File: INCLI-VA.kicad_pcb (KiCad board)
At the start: 2 copper layers, 100 x 70 mm, 155 parts, among them J1 MSTB 2,5/5-GF-5,08, J2 MSTB 2,5/2-GF-5,08, J401 USB4105-GF-A, J402 UART0, Q101 STD18NF25, Q102 IPD30N10S3L-34, Q701 FDD7N25LZ, Q702 BC817-40, Q703 BC807-40, Q751 FDD7N25LZ, Q752 BC817-40, Q753 BC807-40, SW401 RESET, SW402 BOOT, U1 ADM3055E, U101 LM74930QRGERQ1, U201 TPS7A1650QDGNRQ1, U202 ISO7763FQDWRQ1, U301 TPS62A02QDRLRQ1, U302 LP5907QMFX-3.3Q1, U401 ESP32-S3-WROOM-1-N8R2, U402 USBLC6-2SC6, U501 SCL3300-D01, U502 ASM330LHHTR, U503 AS5147U-HTSM

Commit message: [Claude Code] DRU para JLCPCB, red U101_RTN y limpieza de librerías
- INCLI-VA.kicad_dru: capacidades de JLCPCB (2 capas, 1 oz, 1.6 mm) con
  margen; separación HV en la entrada (1.25 mm, IPC-2221B B2), DO y
  +VPROT (0.6 mm); barrera del ADM3055E (2.5 mm + sin relleno bajo U601);
  anchos IPC-2152 (entrada 1.0 mm, DO y 5 V 0.5 mm); reglas para el pad 25
  de U101 (aislado y nunca GND, probado en una copia).
- U101 pin 25 (EP): no_connect -> passive en la librería y la caché;
  etiqueta U101_RTN en 10_power_input. En el PCB, las 7 redes
  unconnected-(U101-EP-Pad25)_N quedan como /10_power_input/U101_RTN
  (sin Update PCB from Schematic).
- Se borran las huellas y modelos 3D de URB2405 y HVSSOP-8, fp-lib-table.bak
  y lib/Connector_Phoenix_MSTB.pretty.bak/.
- PENDIENTES: reglas y fuentes, estado del DRC, propuesta de la hoja 80.

Co-Authored-By: Claude Opus 5.5 <noreply@anthropic.com>
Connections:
- U101 pad 25: unconnected-(U101-EP-Pad25) -> /10_power_input/U101_RTN
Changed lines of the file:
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@@
 			(layers "*.Cu")
 			(remove_unused_layers no)
-			(net "unconnected-(U101-EP-Pad25)_2")
+			(net "/10_power_input/U101_RTN")
 			(pinfunction "EP_25")
-			(pintype "no_connect")
+			(pintype "passive")
 		)
 		(pad "25" thru_hole circle
@@
 			(layers "*.Cu")
 			(remove_unused_layers no)
-			(net "unconnected-(U101-EP-Pad25)_1")
+			(net "/10_power_input/U101_RTN")
 			(pinfunction "EP_25")
-			(pintype "no_connect")
+			(pintype "passive")
 		)
 		(pad "25" thru_hole circle
@@
 			(layers "*.Cu")
 			(remove_unused_layers no)
-			(net "unconnected-(U101-EP-Pad25)_5")
+			(net "/10_power_input/U101_RTN")
 			(pinfunction "EP_25")
-			(pintype "no_connect")
+			(pintype "passive")
 		)
 		(pad "25" smd rect
@@
 			(size 2.1 2.1)
 			(layers "F.Cu" "F.Mask")
-			(net "unconnected-(U101-EP-Pad25)_4")
+			(net "/10_power_input/U101_RTN")
 			(pinfunction "EP_25")
-			(pintype "no_connect")
+			(pintype "passive")
 			(zone_connect 2)
 		)
@@
 			(size 2.4 2.4)
 			(layers "B.Cu" "B.Mask")
-			(net "unconnected-(U101-EP-Pad25)_6")
+			(net "/10_power_input/U101_RTN")
 			(pinfunction "EP_25")
-			(pintype "no_connect")
+			(pintype "passive")
 		)
 		(pad "25" thru_hole circle
@@
 			(layers "*.Cu")
 			(remove_unused_layers no)
-			(net "unconnected-(U101-EP-Pad25)_3")
+			(net "/10_power_input/U101_RTN")
 			(pinfunction "EP_25")
-			(pintype "no_connect")
+			(pintype "passive")
 		)
 		(pad "25" thru_hole circle
@@
 			(layers "*.Cu")
 			(remove_unused_layers no)
-			(net "unconnected-(U101-EP-Pad25)")
+			(net "/10_power_input/U101_RTN")
 			(pinfunction "EP_25")
-			(pintype "no_connect")
+			(pintype "passive")
 		)
 		(embedded_fonts no)

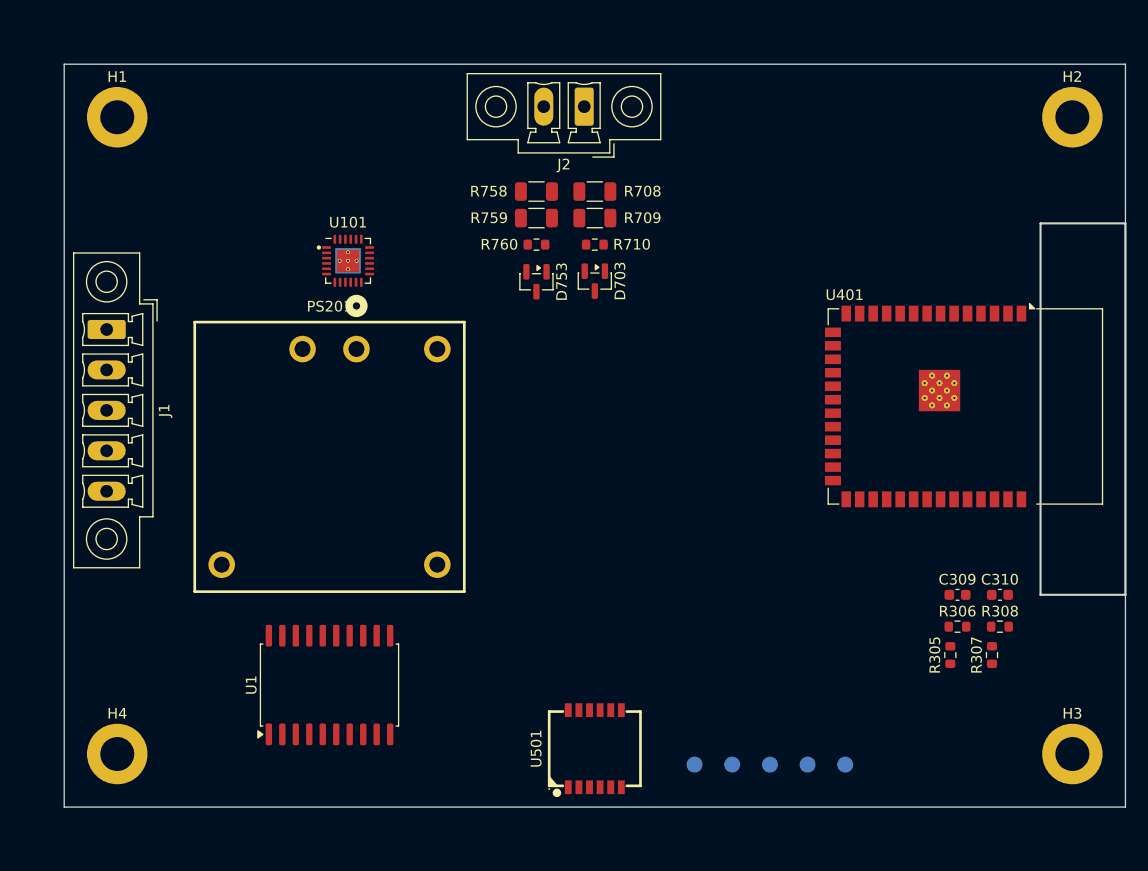
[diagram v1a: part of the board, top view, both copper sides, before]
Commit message: [Claude Code] 80_supervision: TPS3828-33-Q1, LED y VAR_ID; J1/J2 verticales; contorno con muesca
- 80_supervision: U801 TPS3828-33QDBVRQ1 (supervisor de +3V3_D + watchdog,
  WDI <- IO17), R802 0 ohm, R801 DNP; LED verde/rojo DNP en PROD (caja
  opaca); VAR_ID0/1 (CAN/OUT) y VAR_ID2 (IO8, CABIN, DNP).
- WD_EN eliminado (IO18 libre); VAR_ID2 ocupa su pin en las hojas 40/80 y la raíz.
- 10_power_input: J1/J2 MSTBV 2,5 GF 5.08 verticales (1777109 / 1777073).
- lib: se borran los símbolos URB2405 y TPS7A1650; U101: vías del EP a Ø 0.45 mm.
- PCB: contorno único con muesca de 8 x 35 mm para la antena (antes, dos
  rectángulos superpuestos); serigrafía de U401 recortada en la muesca.
- ERC: 0 errores, 1 aviso intencional (U101_RTN).

Co-Authored-By: Claude Opus 5.5 <noreply@anthropic.com>
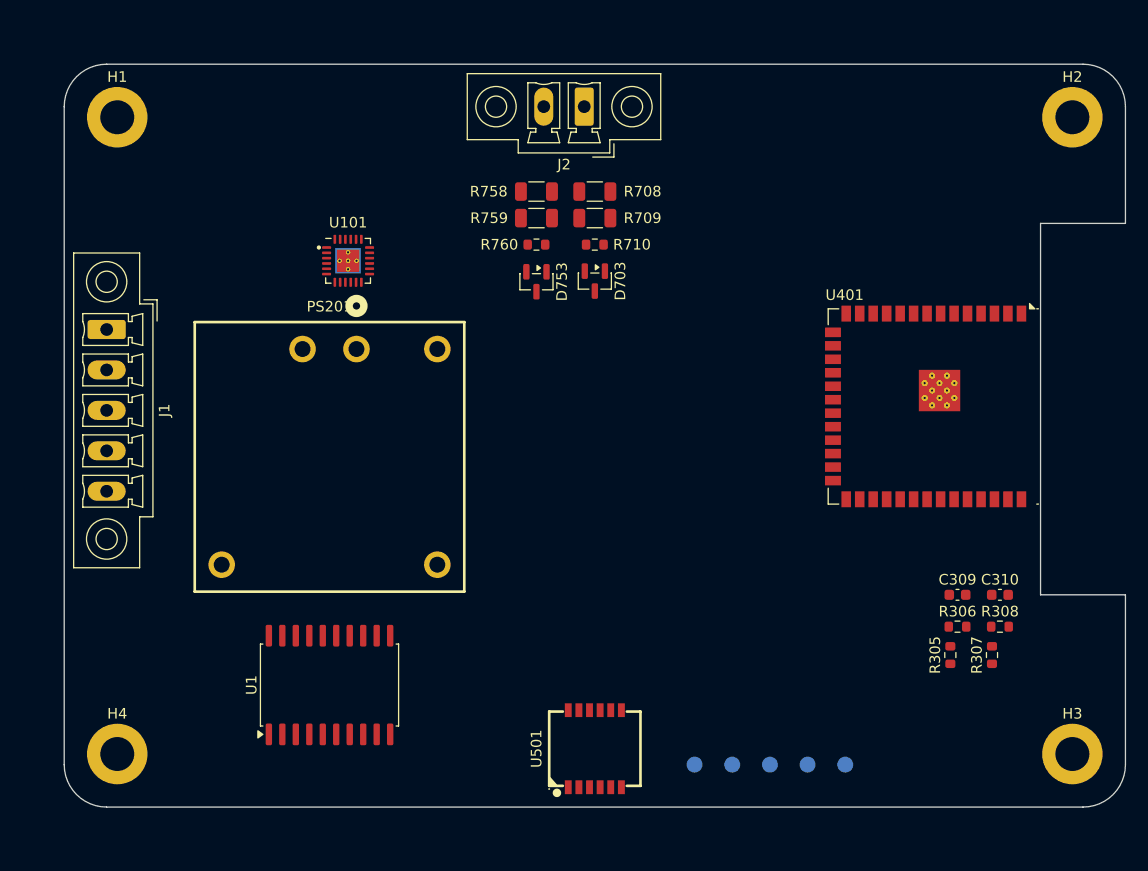
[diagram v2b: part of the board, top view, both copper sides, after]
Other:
- outline, holes or cut-outs redrawn
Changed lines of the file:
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@@
 		(layer "F.Cu")
 		(at 126.75 68.525)
-		(descr "TI LM74930-Q1 RGE0024T VQFN-24 4x4 mm, P0.5 mm, EP 2.1 mm. Fuente: datasheet TI SNOSDF6 (Oct 2023), Example Board Layout / Stencil 4228214/A. Pads alargados a 0.85 mm (TI 0.6) con el mismo borde interior para soldar a mano. Pasta del EP en 4x 0.94 mm (77 %%). 5 vias dia 0.2 mm en el EP hacia una isla aislada en B.Cu: el EP es RTN y TI pide dejarlo flotante, NO conectar a GND.")
+		(descr "TI LM74930-Q1 RGE0024T VQFN-24 4x4 mm, P0.5 mm, EP 2.1 mm. Fuente: datasheet TI SNOSDF6 (Oct 2023), Example Board Layout / Stencil 4228214/A. Pads alargados a 0.85 mm (TI 0.6) con el mismo borde interior para soldar a mano. Pasta del EP en 4x 0.94 mm (77 %%). 5 vias en el EP (hueco 0.2 mm, Ø 0.45 mm: sin recargo en JLCPCB) hacia una isla aislada en B.Cu: el EP es RTN y TI pide dejarlo flotante, NO conectar a GND.")
 		(tags "VQFN-24 RGE0024T LM74930 thermal vias hand solder")
 		(property "Reference" "U101"
@@
 		(pad "25" thru_hole circle
 			(at -0.8 0)
-			(size 0.4 0.4)
+			(size 0.45 0.45)
 			(drill 0.2)
 			(layers "*.Cu")
@@
 		(pad "25" thru_hole circle
 			(at 0 -0.8)
-			(size 0.4 0.4)
+			(size 0.45 0.45)
 			(drill 0.2)
 			(layers "*.Cu")
@@
 		(pad "25" thru_hole circle
 			(at 0 0)
-			(size 0.4 0.4)
+			(size 0.45 0.45)
 			(drill 0.2)
 			(layers "*.Cu")
@@
 		(pad "25" thru_hole circle
 			(at 0 0.8)
-			(size 0.4 0.4)
+			(size 0.45 0.45)
 			(drill 0.2)
 			(layers "*.Cu")
@@
 		(pad "25" thru_hole circle
 			(at 0.8 0)
-			(size 0.4 0.4)
+			(size 0.45 0.45)
 			(drill 0.2)
 			(layers "*.Cu")
@@
 		)
 		(fp_line
-			(start -9.2 -12.9)
+			(start -9.2 -6.86)
 			(end -9.2 -6.7)
 			(stroke
@@
 		)
 		(fp_line
-			(start -9.2 -12.9)
-			(end 9.2 -12.9)
-			(stroke
-				(width 0.12)
-				(type solid)
-			)
-			(layer "F.SilkS")
-		)
-		(fp_line
-			(start 9.2 -12.9)
+			(start 9.2 -6.86)
 			(end 9.2 -6.7)
 			(stroke
@@
 		(embedded_fonts no)
 	)
-	(gr_rect
-		(start 100 50)
-		(end 200 120)
-		(radius 4)
+	(gr_line
+		(start 104 50)
+		(end 196 50)
+		(stroke
+			(width 0.1)
+			(type solid)
+		)
+		(locked yes)
+		(layer "Edge.Cuts")
+	)
+	(gr_arc
+		(start 196 50)
+		(mid 198.8284 51.1716)
+		(end 200 54)
 		(stroke
 			(width 0.1)
 			(type solid)
 		)
-		(fill no)
 		(locked yes)
 		(layer "Edge.Cuts")
 	)
-	(gr_rect
+	(gr_line
+		(start 200 54)
+		(end 200 65)
+		(stroke
+			(width 0.1)
+			(type solid)
+		)
+		(locked yes)
+		(layer "Edge.Cuts")
+	)
+	(gr_line
+		(start 200 65)
+		(end 192 65)
+		(stroke
+			(width 0.1)
+			(type solid)
+		)
+		(locked yes)
+		(layer "Edge.Cuts")
+	)
+	(gr_line
 		(start 192 65)
+		(end 192 100)
+		(stroke
+			(width 0.1)
+			(type solid)
+		)
+		(locked yes)
+		(layer "Edge.Cuts")
+	)
+	(gr_line
+		(start 192 100)
 		(end 200 100)
 		(stroke
-			(width 0.2)
+			(width 0.1)
+			(type solid)
+		)
+		(locked yes)
+		(layer "Edge.Cuts")
+	)
+	(gr_line
+		(start 200 100)
+		(end 200 116)
+		(stroke
+			(width 0.1)
+			(type solid)
+		)
+		(locked yes)
+		(layer "Edge.Cuts")
+	)
+	(gr_arc
+		(start 200 116)
+		(mid 198.8284 118.8284)
+		(end 196 120)
+		(stroke
+			(width 0.1)
+			(type solid)
+		)
+		(locked yes)
+		(layer "Edge.Cuts")
+	)
+	(gr_line
+		(start 196 120)
+		(end 104 120)
+		(stroke
+			(width 0.1)
+			(type solid)
+		)
+		(locked yes)
+		(layer "Edge.Cuts")
+	)
+	(gr_arc
+		(start 104 120)
+		(mid 101.1716 118.8284)
+		(end 100 116)
+		(stroke
+			(width 0.1)
+			(type solid)
+		)
+		(locked yes)
+		(layer "Edge.Cuts")
+	)
+	(gr_line
+		(start 100 116)
+		(end 100 54)
+		(stroke
+			(width 0.1)
+			(type solid)
+		)
+		(locked yes)
+		(layer "Edge.Cuts")
+	)
+	(gr_arc
+		(start 100 54)
+		(mid 101.1716 51.1716)
+		(end 104 50)
+		(stroke
+			(width 0.1)
 			(type solid)
 		)
-		(fill no)
 		(locked yes)
 		(layer "Edge.Cuts")
